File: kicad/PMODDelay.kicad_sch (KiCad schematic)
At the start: 9 parts, among them J1 Conn_02x06_Counter_Clockwise_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, U1 TPS61222DCK

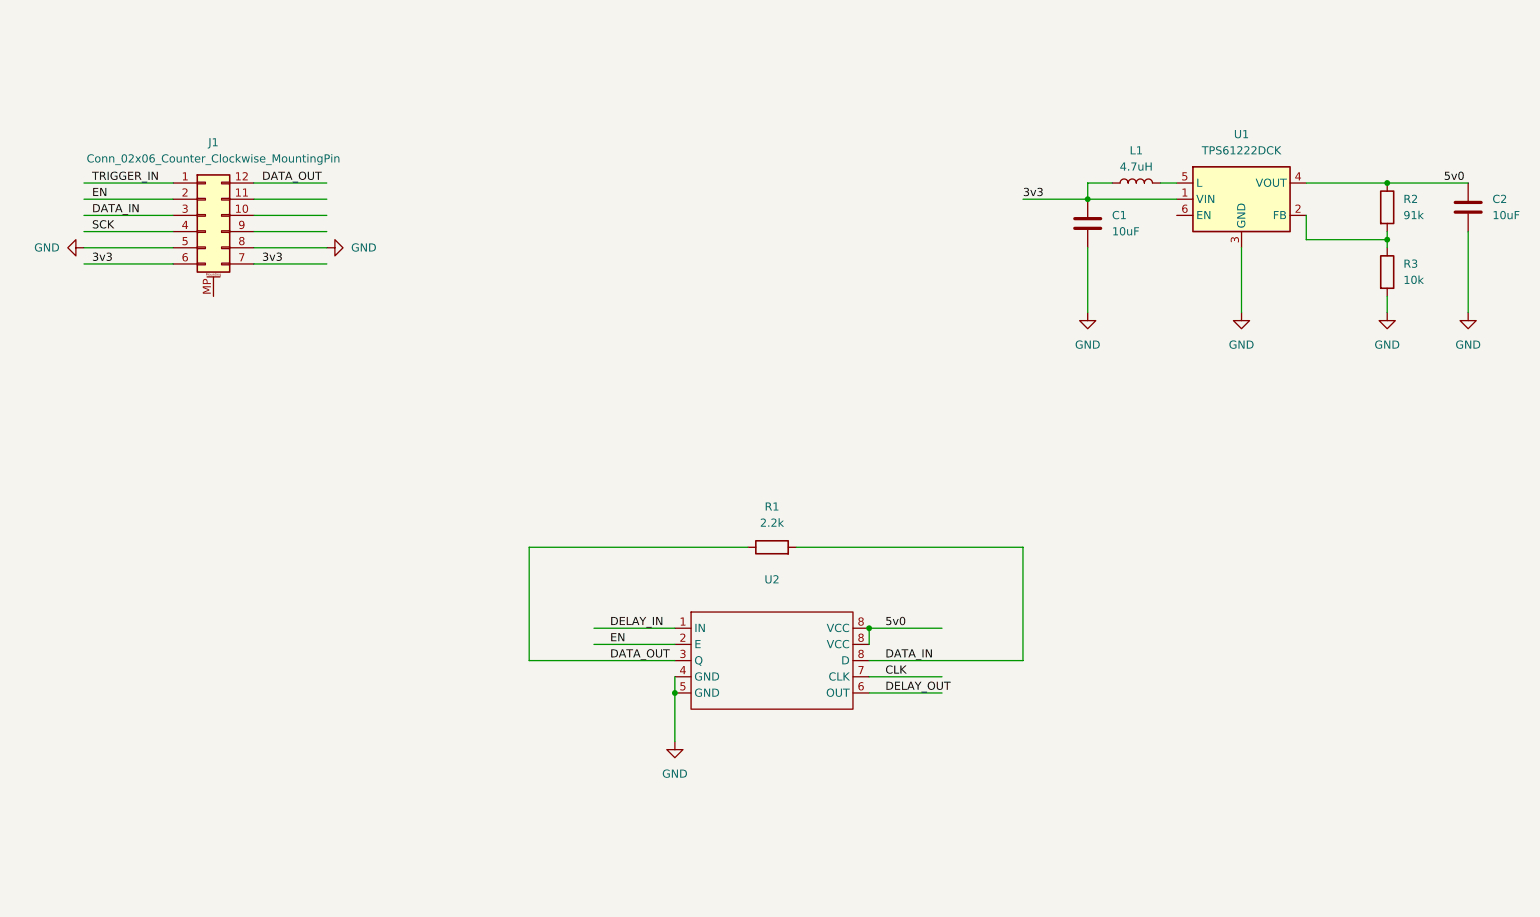
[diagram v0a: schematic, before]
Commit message: Introducing DS1124U Driver, updating PCB.
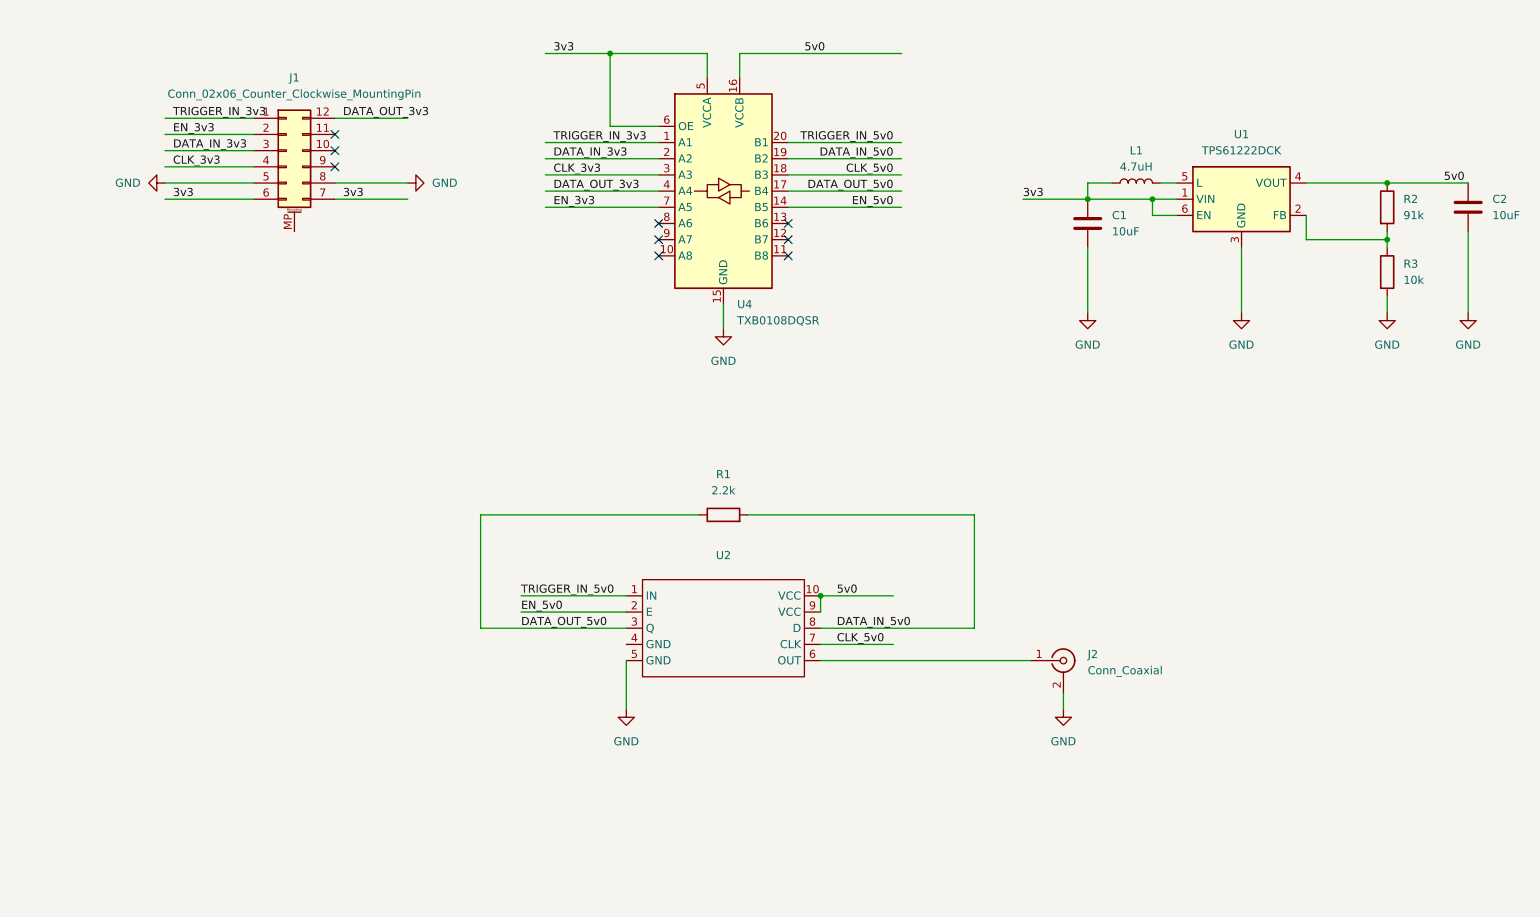
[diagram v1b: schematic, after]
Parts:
- added J2: Conn_Coaxial, Connector_Coaxial:SMA_Amphenol_901-144_Vertical, symbol Connector:Conn_Coaxial
- added U4: TXB0108DQSR, Package_SON:USON-20_2x4mm_P0.4mm, symbol Logic_LevelTranslator:TXB0108DQSR
- C1, C2: footprint (none) -> Capacitor_SMD:C_0805_2012Metric
- L1, R1, R2, R3: footprint (none) -> Resistor_SMD:R_0805_2012Metric
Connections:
- net 3v3: now also U1.6 (EN), U4.5 (VCCA), U4.6 (OE)
- net 5v0: now also U2.10 (VCC), U2.9 (VCC), U4.16 (VCCB); no longer U2.8 (D)
- net GND: now also J2.2 (Ext), U4.15 (GND); no longer U2.4 (GND)
- net CLK renamed CLK_5v0
- net CLK_5v0: now also U4.18 (B3)
- net DATA_IN renamed DATA_IN_5v0
- net DATA_IN_5v0: now also U4.19 (B2); no longer J1.3 (Pin_3)
- net DATA_OUT renamed DATA_OUT_5v0
- net DATA_OUT_5v0: now also U4.17 (B4); no longer J1.12 (Pin_12)
- net DELAY_IN renamed TRIGGER_IN_5v0
- net TRIGGER_IN_5v0: now also U4.20 (B1)
- net DELAY_OUT: no longer names the net of U2.6 (OUT)
- net DELAY_OUT: now also J2.1 (In)
- net EN renamed EN_3v3
- net EN_3v3: now also U4.7 (A5); no longer U2.2 (E)
- net SCK renamed CLK_3v3
- net CLK_3v3: now also U4.3 (A3)
- net TRIGGER_IN renamed TRIGGER_IN_3v3
- net TRIGGER_IN_3v3: now also U4.1 (A1)
- new net DATA_IN_3v3: J1.3 (Pin_3), U4.2 (A2)
- new net DATA_OUT_3v3: J1.12 (Pin_12), U4.4 (A4)
- new net EN_5v0: U2.2 (E), U4.14 (B5)
- no-connect marks 0 -> 9
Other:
- moved on the sheet: J1, R1

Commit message: Updating Schematic
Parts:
- removed J1: Conn_02x06_Counter_Clockwise_MountingPin, symbol Connector_Generic_MountingPin:Conn_02x06_Counter_Clockwise_MountingPin
- added C3, C4, C5: 10uF, Capacitor_SMD:C_0805_2012Metric_Pad1.18x1.45mm_HandSolder, symbol Device:C
- added C6: 1uF, Capacitor_SMD:C_0805_2012Metric_Pad1.18x1.45mm_HandSolder, symbol Device:C
- added J1: Conn_02x06_Odd_Even, Connector_PinHeader_2.54mm:PinHeader_2x06_P2.54mm_Horizontal, symbol Connector_Generic:Conn_02x06_Odd_Even
- added J3: TRIG_3v3, Connector_Coaxial:SMA_Amphenol_901-144_Vertical, symbol Connector:Conn_Coaxial
- added R4: 1.8k, Resistor_SMD:R_0805_2012Metric_Pad1.20x1.40mm_HandSolder, symbol Device:R
- added R5: 3.3k, Resistor_SMD:R_0805_2012Metric_Pad1.20x1.40mm_HandSolder, symbol Device:R
- J2: value Conn_Coaxial -> TRIG_5v0
- R1: value 2.2k -> 4.7k
- U2: footprint (none) -> Package_SO:TSSOP-10_3x3mm_P0.5mm
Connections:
- net 3v3: now also C3.1, J1.11 (Pin_11), J1.12 (Pin_12)
- net 5v0: now also C4.1, C5.1, C6.1
- net CLK_3v3: now also J1.7 (Pin_7)
- net DATA_IN_3v3: now also J1.5 (Pin_5)
- net DATA_OUT_3v3: now also J1.2 (Pin_2)
- net EN_3v3: now also J1.3 (Pin_3)
- net GND: now also U2.4 (GND), C3.2, C4.2, C5.2, C6.2, J1.10 (Pin_10), J1.9 (Pin_9), J3.2 (Ext), R5.2
- net TRIGGER_IN_3v3: now also J1.1 (Pin_1)
- net OUT_5v0: now reaches J2.1 (In), U2.6 (OUT)
- net OUT_5v0: now also R4.1
- new net OUT_3v3: J3.1 (In), R4.2, R5.1
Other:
- moved on the sheet: J2, R1, U2
